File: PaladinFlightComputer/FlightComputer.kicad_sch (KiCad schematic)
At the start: 20 parts, among them J1 Micro_SD_Card_Det1, J3 Conn_01x03, J4 Conn_01x03, J5 Conn_01x03, J6 Screw_Terminal_01x02, J7 Conn_01x03, J8 Conn_01x04, U1 GY-521

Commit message: Paladin Test Push
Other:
- note added: "PALDIN V1.0"
- note removed: "PALDIN"
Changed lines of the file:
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@@
 		)
 	)
-	(text "PALDIN"
+	(text "PALDIN V1.0"
 		(exclude_from_sim no)
-		(at 192.024 189.992 0)
+		(at 195.834 189.738 0)
 		(effects
 			(font

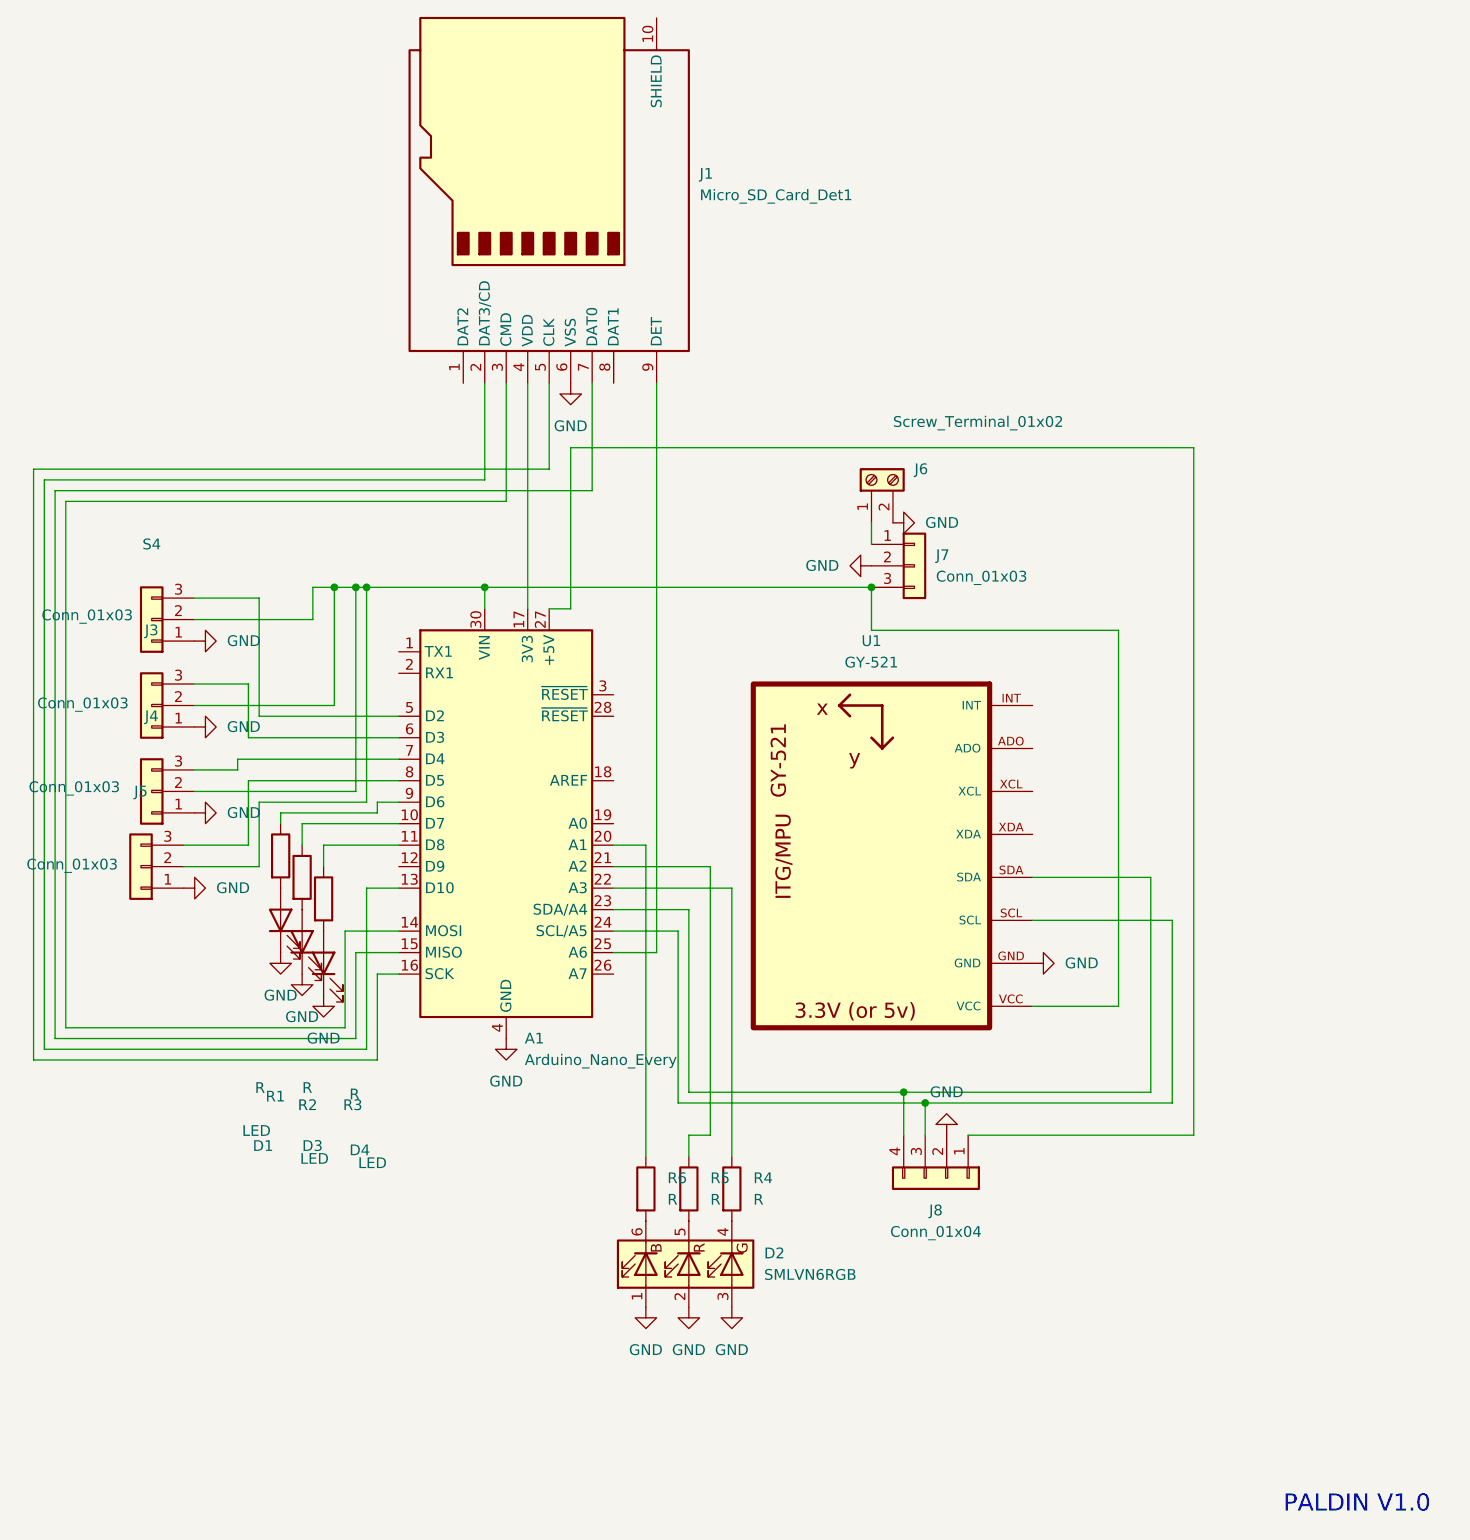
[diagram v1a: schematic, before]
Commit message: dual rgb lights on both sides
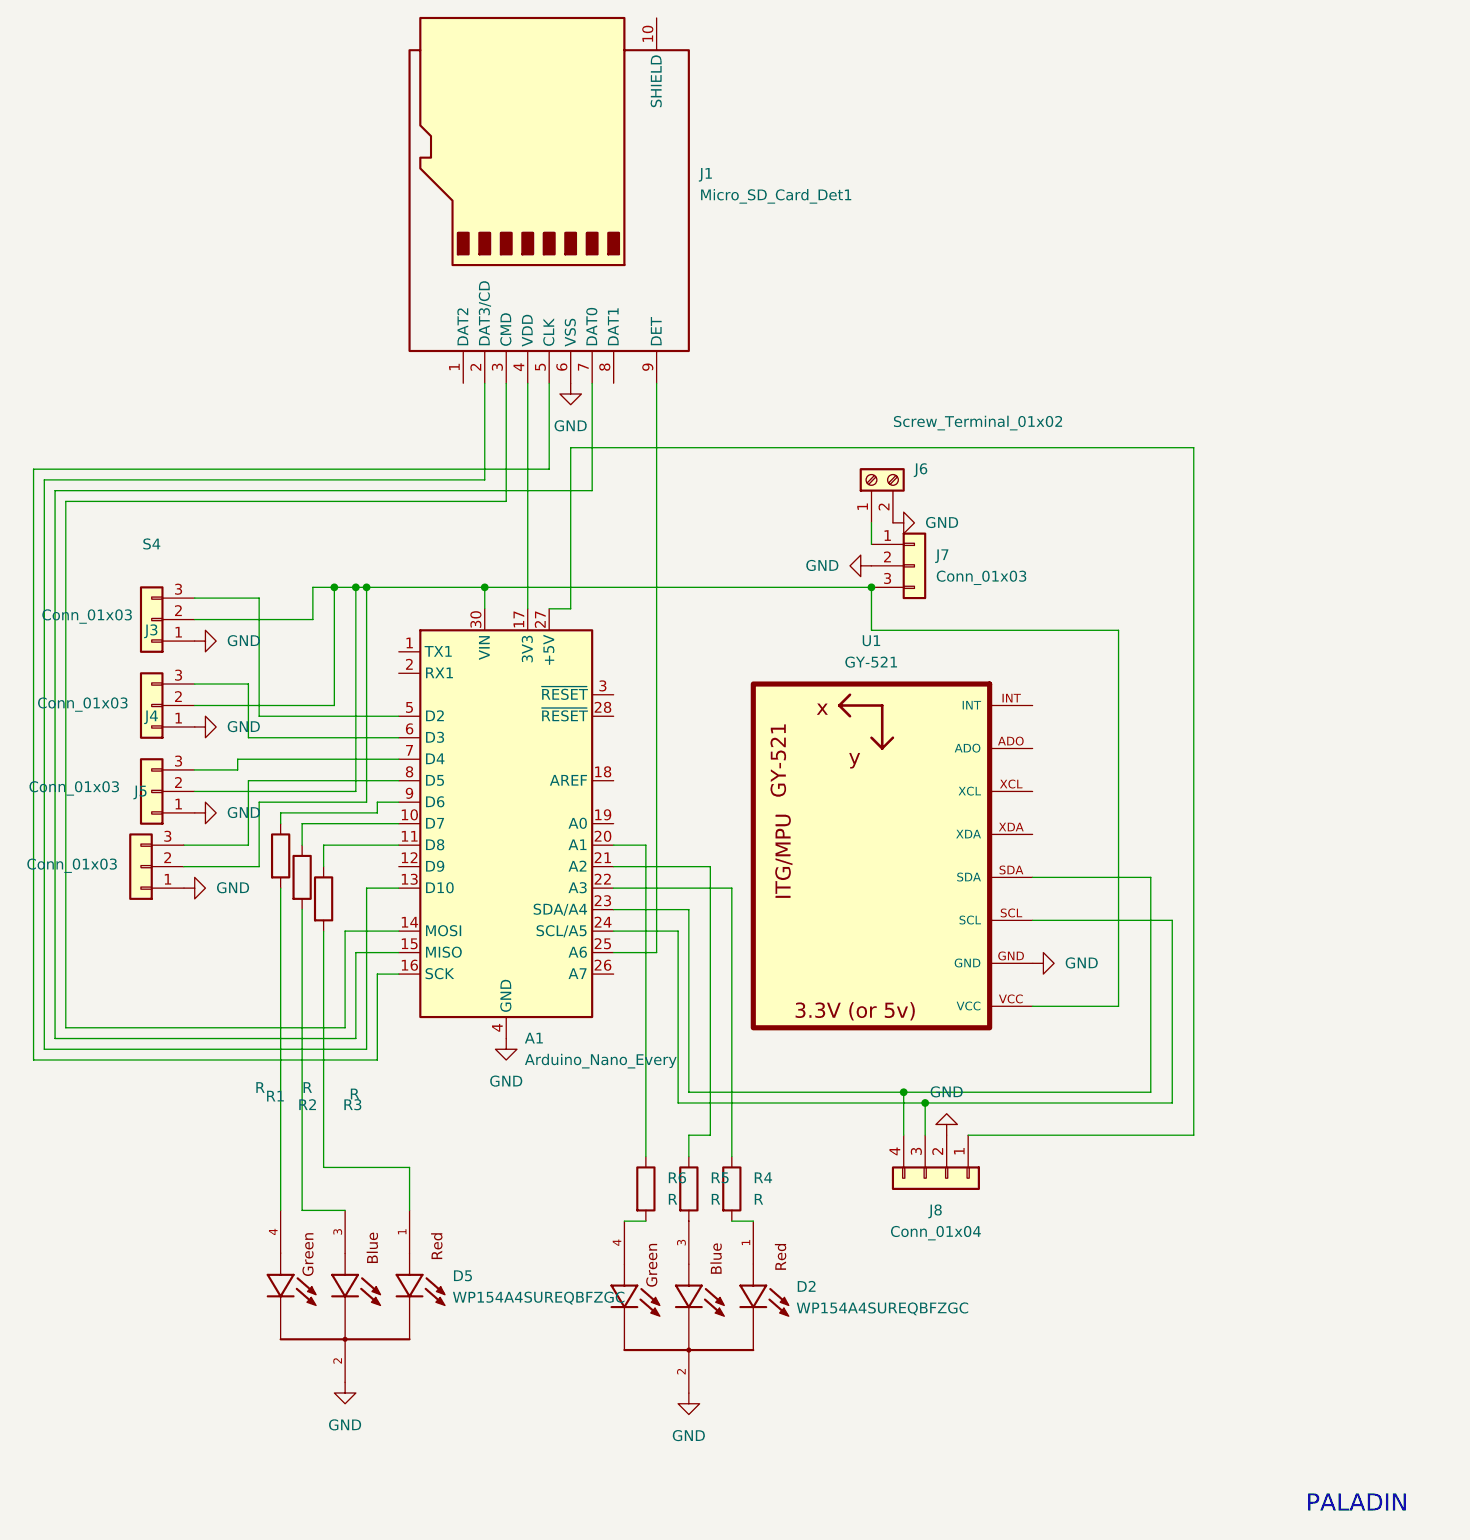
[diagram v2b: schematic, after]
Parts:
- removed D1, D3, D4: LED, LED_THT:LED_D3.0mm, symbol Device:LED
- removed D2: SMLVN6RGB, LED_SMD:LED_ROHM_SMLVN6, symbol LED:SMLVN6RGB
- added D2, D5: WP154A4SUREQBFZGC, WP154A4SUREQBFZGC:LED_WP154A4SUREQBFZGC, symbol WP154A4SUREQBFZGC:WP154A4SUREQBFZGC
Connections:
- net GND: now also D2.2, D5.2
- net at R2.2: now also D5.3
- net at R3.2: now also D5.1
- net at R1.2: now also D5.4
- net at R5.2: now also D2.3
- net at R6.2: now also D2.4
- net at R4.2: now also D2.1
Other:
- note added: "PALADIN"
- note removed: "PALDIN V1.0"
